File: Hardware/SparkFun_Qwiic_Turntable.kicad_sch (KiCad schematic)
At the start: 5 parts

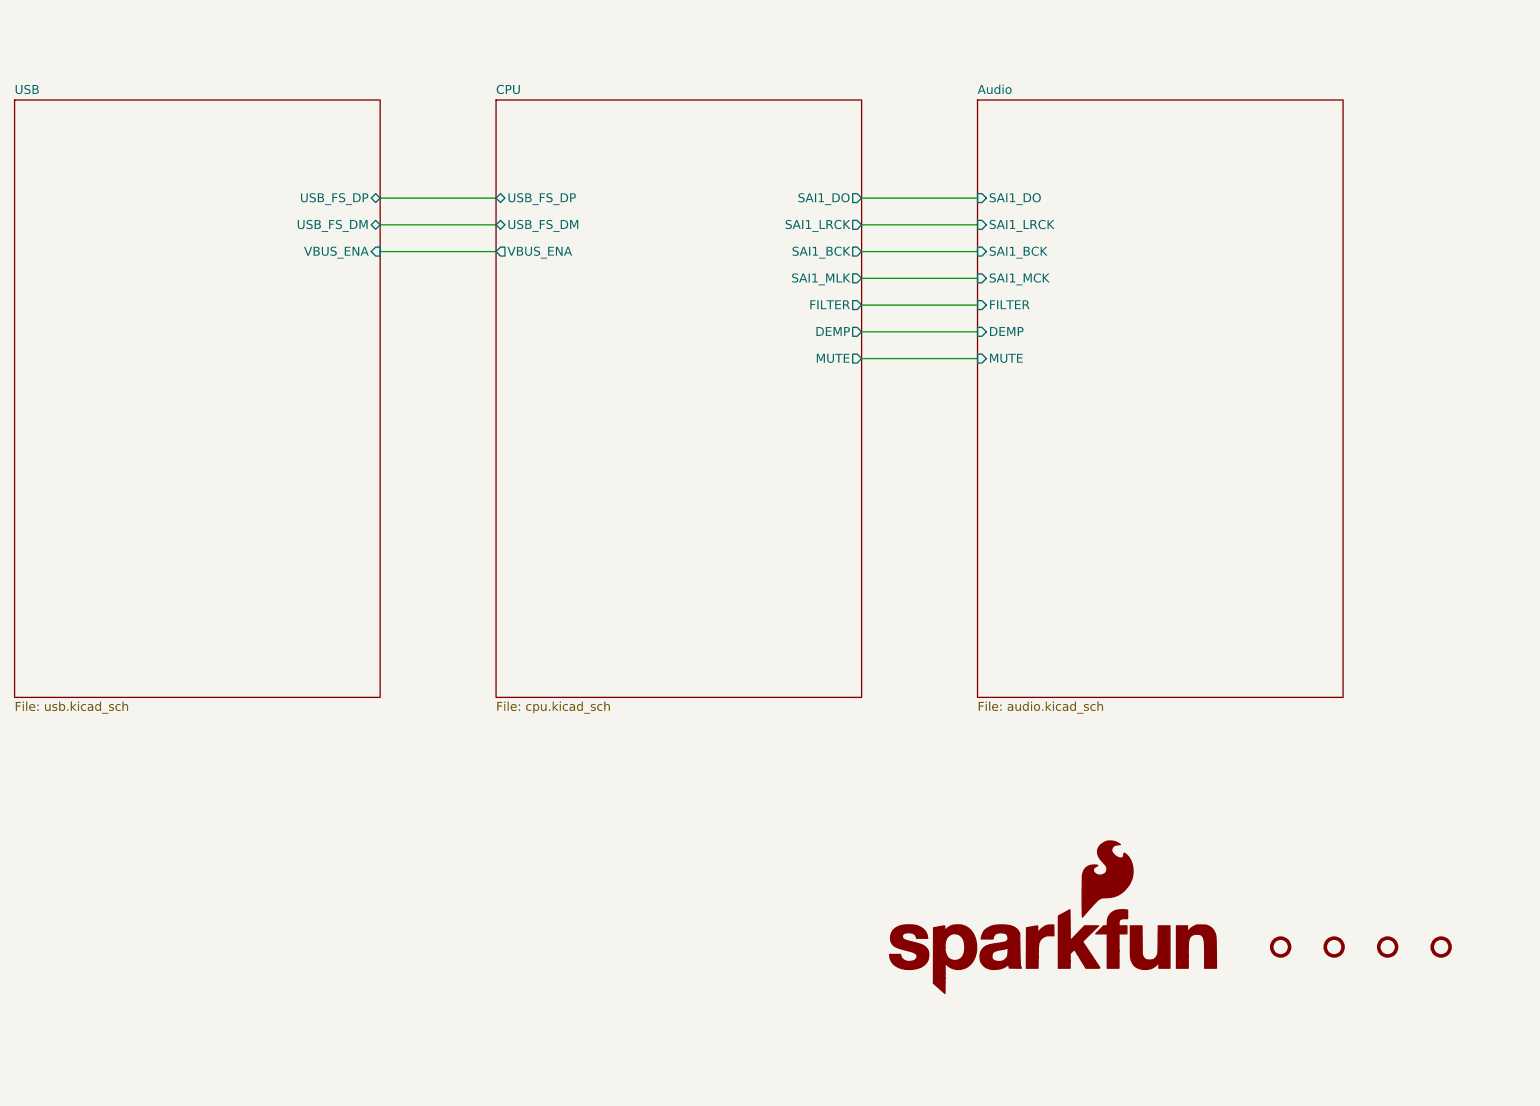
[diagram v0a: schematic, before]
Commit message: Restored VBUS load switch / limit circuit and changed most of the passives to 0402s.
Signed-off-by: Jamie Robertson <jrr@robertsonics.com>
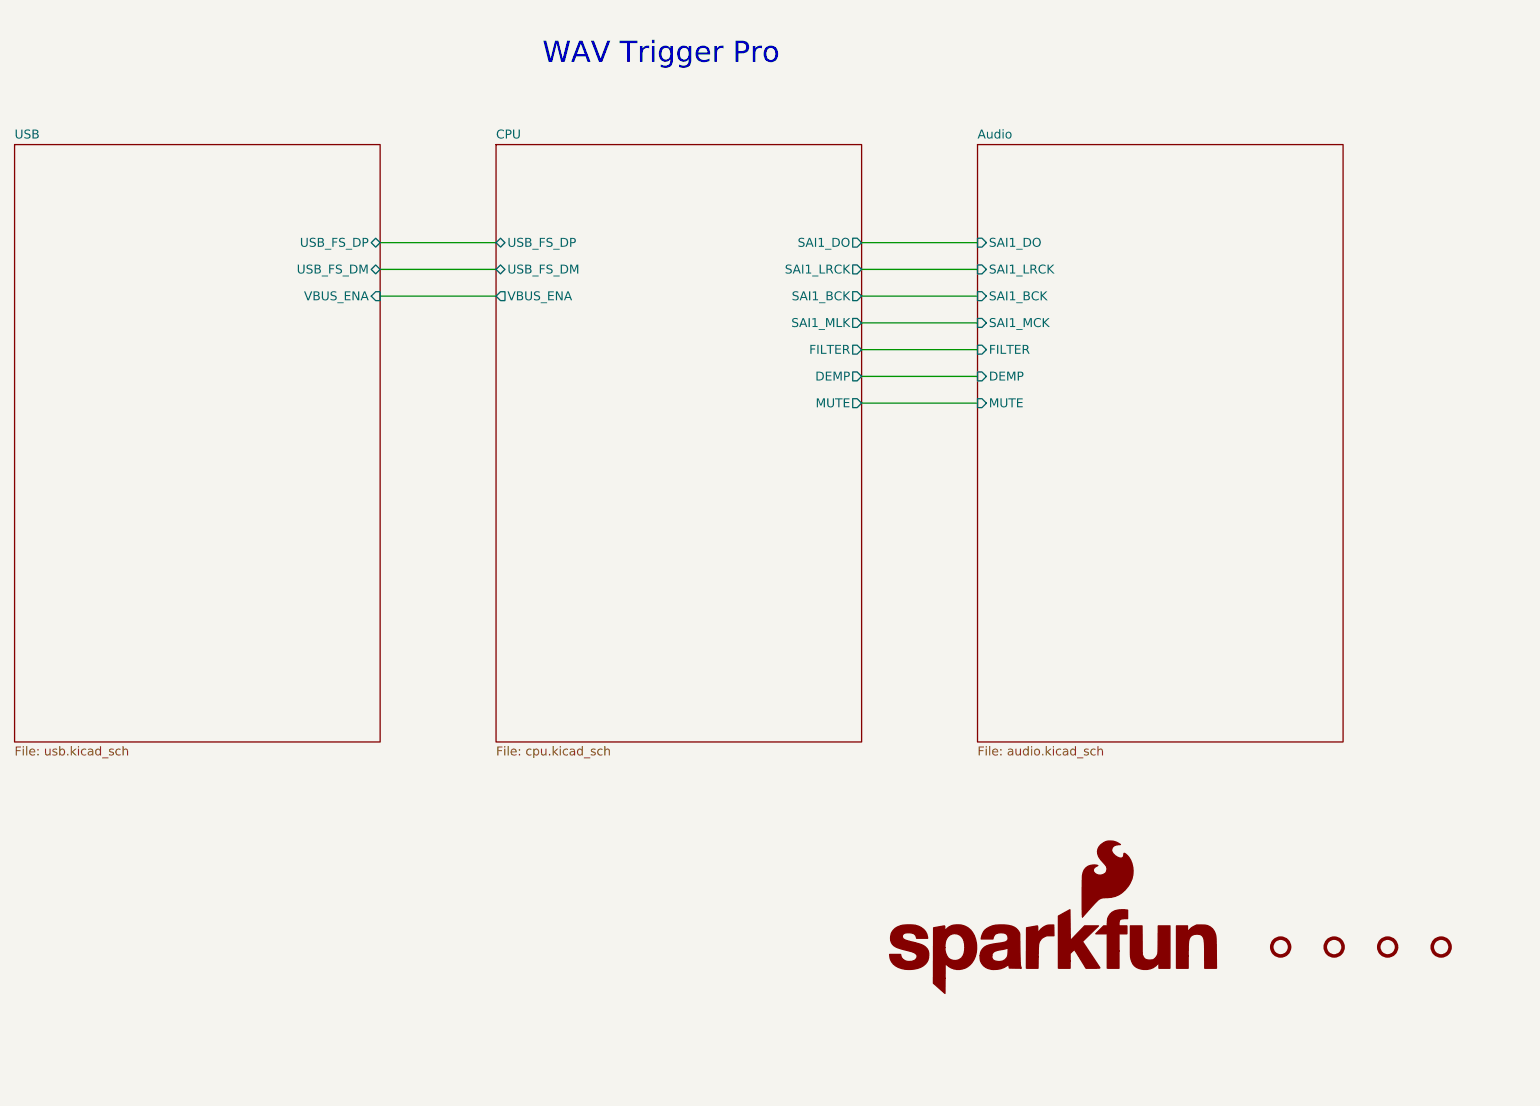
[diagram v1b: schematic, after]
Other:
- note added: "WAV Trigger Pro"
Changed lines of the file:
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@@
 	(wire
 		(pts
-			(xy 166.37 72.39) (xy 182.88 72.39)
-		)
-		(stroke
-			(width 0)
-			(type default)
-		)
-	)
-	(wire
-		(pts
-			(xy 97.79 60.96) (xy 114.3 60.96)
-		)
-		(stroke
-			(width 0)
-			(type default)
-		)
-	)
-	(wire
-		(pts
-			(xy 166.37 60.96) (xy 182.88 60.96)
-		)
-		(stroke
-			(width 0)
-			(type default)
-		)
-	)
-	(wire
-		(pts
-			(xy 97.79 64.77) (xy 114.3 64.77)
-		)
-		(stroke
-			(width 0)
-			(type default)
-		)
-	)
-	(wire
-		(pts
-			(xy 166.37 57.15) (xy 182.88 57.15)
-		)
-		(stroke
-			(width 0)
-			(type default)
-		)
-	)
-	(wire
-		(pts
-			(xy 97.79 57.15) (xy 114.3 57.15)
-		)
-		(stroke
-			(width 0)
-			(type default)
-		)
-	)
-	(wire
-		(pts
-			(xy 166.37 64.77) (xy 182.88 64.77)
-		)
-		(stroke
-			(width 0)
-			(type default)
-		)
-	)
-	(wire
-		(pts
-			(xy 166.37 76.2) (xy 182.88 76.2)
-		)
-		(stroke
-			(width 0)
-			(type default)
-		)
-	)
-	(wire
-		(pts
-			(xy 166.37 80.01) (xy 182.88 80.01)
-		)
-		(stroke
-			(width 0)
-			(type default)
-		)
-	)
-	(wire
-		(pts
-			(xy 166.37 68.58) (xy 182.88 68.58)
-		)
-		(stroke
-			(width 0)
-			(type default)
+			(xy 166.37 78.74) (xy 182.88 78.74)
+		)
+		(stroke
+			(width 0)
+			(type default)
+		)
+	)
+	(wire
+		(pts
+			(xy 97.79 67.31) (xy 114.3 67.31)
+		)
+		(stroke
+			(width 0)
+			(type default)
+		)
+	)
+	(wire
+		(pts
+			(xy 166.37 67.31) (xy 182.88 67.31)
+		)
+		(stroke
+			(width 0)
+			(type default)
+		)
+	)
+	(wire
+		(pts
+			(xy 97.79 71.12) (xy 114.3 71.12)
+		)
+		(stroke
+			(width 0)
+			(type default)
+		)
+	)
+	(wire
+		(pts
+			(xy 166.37 63.5) (xy 182.88 63.5)
+		)
+		(stroke
+			(width 0)
+			(type default)
+		)
+	)
+	(wire
+		(pts
+			(xy 97.79 63.5) (xy 114.3 63.5)
+		)
+		(stroke
+			(width 0)
+			(type default)
+		)
+	)
+	(wire
+		(pts
+			(xy 166.37 71.12) (xy 182.88 71.12)
+		)
+		(stroke
+			(width 0)
+			(type default)
+		)
+	)
+	(wire
+		(pts
+			(xy 166.37 82.55) (xy 182.88 82.55)
+		)
+		(stroke
+			(width 0)
+			(type default)
+		)
+	)
+	(wire
+		(pts
+			(xy 166.37 86.36) (xy 182.88 86.36)
+		)
+		(stroke
+			(width 0)
+			(type default)
+		)
+	)
+	(wire
+		(pts
+			(xy 166.37 74.93) (xy 182.88 74.93)
+		)
+		(stroke
+			(width 0)
+			(type default)
+		)
+	)
+	(text "WAV Trigger Pro"
+		(exclude_from_sim no)
+		(at 120.904 38.354 0)
+		(effects
+			(font
+				(size 3 3)
+			)
+			(justify left bottom)
 		)
 	)
@@
 	)
 	(sheet
-		(at 114.3 43.18)
+		(at 114.3 49.53)
 		(size 52.07 85.09)
 		(fields_autoplaced yes)
@@
 		)
 		(property "Sheetname" "CPU"
-			(at 114.3 42.4684 0)
+			(at 114.3 48.8184 0)
 			(effects
 				(font
@@
 		)
 		(property "Sheetfile" "cpu.kicad_sch"
-			(at 114.3 128.8546 0)
+			(at 114.3 135.2046 0)
 			(effects
 				(font
@@
 		)
 		(pin "SAI1_DO" output
-			(at 166.37 57.15 0)
+			(at 166.37 63.5 0)
 			(effects
 				(font
@@
 		)
 		(pin "SAI1_LRCK" output
-			(at 166.37 60.96 0)
+			(at 166.37 67.31 0)
 			(effects
 				(font
@@
 		)
 		(pin "SAI1_BCK" output
-			(at 166.37 64.77 0)
+			(at 166.37 71.12 0)
 			(effects
 				(font
@@
 		)
 		(pin "SAI1_MLK" output
-			(at 166.37 68.58 0)
+			(at 166.37 74.93 0)
 			(effects
 				(font
@@
 		)
 		(pin "USB_FS_DM" bidirectional
-			(at 114.3 60.96 180)
+			(at 114.3 67.31 180)
 			(effects
 				(font
@@
 		)
 		(pin "VBUS_ENA" output
-			(at 114.3 64.77 180)
+			(at 114.3 71.12 180)
 			(effects
 				(font
@@
 		)
 		(pin "USB_FS_DP" bidirectional
-			(at 114.3 57.15 180)
+			(at 114.3 63.5 180)
 			(effects
 				(font
@@
 		)
 		(pin "FILTER" output
-			(at 166.37 72.39 0)
+			(at 166.37 78.74 0)
 			(effects
 				(font
@@
 		)
 		(pin "DEMP" output
-			(at 166.37 76.2 0)
+			(at 166.37 82.55 0)
 			(effects
 				(font
@@
 		)
 		(pin "MUTE" output
-			(at 166.37 80.01 0)
+			(at 166.37 86.36 0)
 			(effects
 				(font
@@
 	)
 	(sheet
-		(at 45.72 43.18)
+		(at 45.72 49.53)
 		(size 52.07 85.09)
 		(fields_autoplaced yes)
@@
 		)
 		(property "Sheetname" "USB"
-			(at 45.72 42.4684 0)
+			(at 45.72 48.8184 0)
 			(effects
 				(font
@@
 		)
 		(property "Sheetfile" "usb.kicad_sch"
-			(at 45.72 128.8546 0)
+			(at 45.72 135.2046 0)
 			(effects
 				(font
@@
 			)
 		)
+		(pin "VBUS_ENA" input
+			(at 97.79 71.12 0)
+			(effects
+				(font
+					(size 1.27 1.27)
+				)
+				(justify right)
+			)
+		)
+		(pin "USB_FS_DM" bidirectional
+			(at 97.79 67.31 0)
+			(effects
+				(font
+					(size 1.27 1.27)
+				)
+				(justify right)
+			)
+		)
 		(pin "USB_FS_DP" bidirectional
-			(at 97.79 57.15 0)
-			(effects
-				(font
-					(size 1.27 1.27)
-				)
-				(justify right)
-			)
-		)
-		(pin "USB_FS_DM" bidirectional
-			(at 97.79 60.96 0)
-			(effects
-				(font
-					(size 1.27 1.27)
-				)
-				(justify right)
-			)
-		)
-		(pin "VBUS_ENA" input
-			(at 97.79 64.77 0)
+			(at 97.79 63.5 0)
 			(effects
 				(font
@@
 	)
 	(sheet
-		(at 182.88 43.18)
+		(at 182.88 49.53)
 		(size 52.07 85.09)
 		(fields_autoplaced yes)
@@
 		)
 		(property "Sheetname" "Audio"
-			(at 182.88 42.4684 0)
+			(at 182.88 48.8184 0)
 			(effects
 				(font
@@
 		)
 		(property "Sheetfile" "audio.kicad_sch"
-			(at 182.88 128.8546 0)
+			(at 182.88 135.2046 0)
 			(effects
 				(font
@@
 		)
 		(pin "SAI1_LRCK" input
-			(at 182.88 60.96 180)
+			(at 182.88 67.31 180)
 			(effects
 				(font
@@
 		)
 		(pin "SAI1_DO" input
-			(at 182.88 57.15 180)
+			(at 182.88 63.5 180)
 			(effects
 				(font
@@
 		)
 		(pin "SAI1_BCK" input
-			(at 182.88 64.77 180)
+			(at 182.88 71.12 180)
 			(effects
 				(font
@@
 		)
 		(pin "SAI1_MCK" input
-			(at 182.88 68.58 180)
+			(at 182.88 74.93 180)
 			(effects
 				(font
@@
 		)
 		(pin "MUTE" input
-			(at 182.88 80.01 180)
+			(at 182.88 86.36 180)
 			(effects
 				(font
@@
 		)
 		(pin "FILTER" input
-			(at 182.88 72.39 180)
+			(at 182.88 78.74 180)
 			(effects
 				(font
@@
 		)
 		(pin "DEMP" input
-			(at 182.88 76.2 180)
-			(effects
-				(font
+			(at 182.88 82.55 180)
+			(effects
+				(font

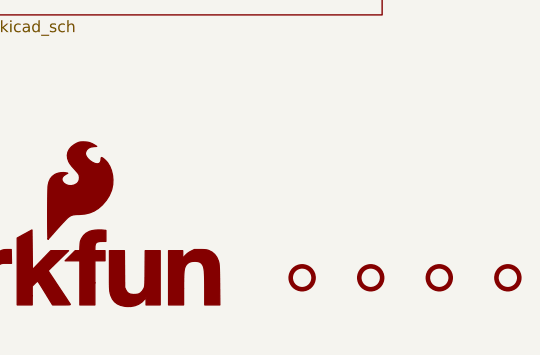
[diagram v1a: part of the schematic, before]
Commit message: Initial parts placement.
Signed-off-by: Jamie Robertson <jrr@robertsonics.com>
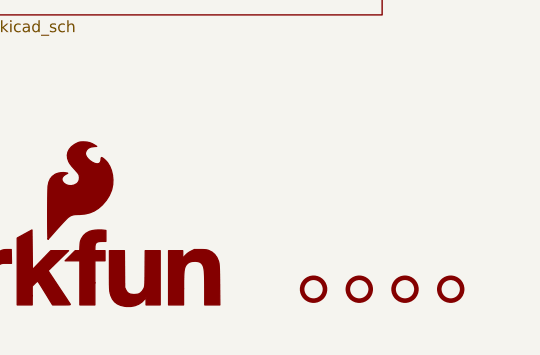
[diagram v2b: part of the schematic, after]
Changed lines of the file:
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@@
 	(symbol
 		(lib_id "SparkFun-Hardware:Standoff")
-		(at 241.3 163.83 0)
+		(at 232.41 165.1 0)
+		(unit 1)
+		(exclude_from_sim no)
+		(in_bom yes)
+		(on_board yes)
+		(dnp no)
+		(fields_autoplaced yes)
+		(property "Reference" "ST2"
+			(at 232.41 162.56 0)
+			(effects
+				(font
+					(size 1.27 1.27)
+				)
+				(hide yes)
+			)
+		)
+		(property "Value" "Standoff"
+			(at 232.41 167.64 0)
+			(effects
+				(font
+					(size 1.27 1.27)
+				)
+				(hide yes)
+			)
+		)
+		(property "Footprint" "SparkFun-Hardware:Standoff"
+			(at 232.41 170.18 0)
+			(effects
+				(font
+					(size 1.27 1.27)
+				)
+				(hide yes)
+			)
+		)
+		(property "Datasheet" "~"
+			(at 232.41 168.91 0)
+			(effects
+				(font
+					(size 1.27 1.27)
+				)
+				(hide yes)
+			)
+		)
+		(property "Description" "Drill holes for mechanically mounting via screws, standoffs, etc."
+			(at 232.41 165.1 0)
+			(effects
+				(font
+					(size 1.27 1.27)
+				)
+				(hide yes)
+			)
+		)
+		(instances
+			(project "SparkFun_Qwiic_Turntable"
+				(path "/4c0b78e3-6801-43aa-85ca-70880324c2bd"
+					(reference "ST2")
+					(unit 1)
+				)
+			)
+		)
+	)
+	(symbol
+		(lib_id "SparkFun-Hardware:Standoff")
+		(at 237.49 165.1 0)
 		(unit 1)
 		(exclude_from_sim no)
@@
 		(fields_autoplaced yes)
 		(property "Reference" "ST3"
-			(at 241.3 161.29 0)
-			(effects
-				(font
-					(size 1.27 1.27)
-				)
-				(hide yes)
-			)
-		)
-		(property "Value" "Standoff"
-			(at 241.3 166.37 0)
-			(effects
-				(font
-					(size 1.27 1.27)
-				)
-				(hide yes)
-			)
-		)
-		(property "Footprint" "SparkFun-Hardware:Standoff"
-			(at 241.3 168.91 0)
-			(effects
-				(font
-					(size 1.27 1.27)
-				)
-				(hide yes)
-			)
-		)
-		(property "Datasheet" "~"
-			(at 241.3 167.64 0)
-			(effects
-				(font
-					(size 1.27 1.27)
-				)
-				(hide yes)
-			)
-		)
-		(property "Description" ""
-			(at 241.3 163.83 0)
+			(at 237.49 162.56 0)
+			(effects
+				(font
+					(size 1.27 1.27)
+				)
+				(hide yes)
+			)
+		)
+		(property "Value" "Standoff"
+			(at 237.49 167.64 0)
+			(effects
+				(font
+					(size 1.27 1.27)
+				)
+				(hide yes)
+			)
+		)
+		(property "Footprint" "SparkFun-Hardware:Standoff"
+			(at 237.49 170.18 0)
+			(effects
+				(font
+					(size 1.27 1.27)
+				)
+				(hide yes)
+			)
+		)
+		(property "Datasheet" "~"
+			(at 237.49 168.91 0)
+			(effects
+				(font
+					(size 1.27 1.27)
+				)
+				(hide yes)
+			)
+		)
+		(property "Description" "Drill holes for mechanically mounting via screws, standoffs, etc."
+			(at 237.49 165.1 0)
 			(effects
 				(font
@@
 	(symbol
 		(lib_id "SparkFun-Hardware:Standoff")
-		(at 226.06 163.83 0)
+		(at 227.33 165.1 0)
 		(unit 1)
 		(exclude_from_sim no)
@@
 		(fields_autoplaced yes)
 		(property "Reference" "ST1"
-			(at 226.06 161.29 0)
-			(effects
-				(font
-					(size 1.27 1.27)
-				)
-				(hide yes)
-			)
-		)
-		(property "Value" "Standoff"
-			(at 226.06 166.37 0)
-			(effects
-				(font
-					(size 1.27 1.27)
-				)
-				(hide yes)
-			)
-		)
-		(property "Footprint" "SparkFun-Hardware:Standoff"
-			(at 226.06 168.91 0)
-			(effects
-				(font
-					(size 1.27 1.27)
-				)
-				(hide yes)
-			)
-		)
-		(property "Datasheet" "~"
-			(at 226.06 167.64 0)
-			(effects
-				(font
-					(size 1.27 1.27)
-				)
-				(hide yes)
-			)
-		)
-		(property "Description" ""
-			(at 226.06 163.83 0)
+			(at 227.33 162.56 0)
+			(effects
+				(font
+					(size 1.27 1.27)
+				)
+				(hide yes)
+			)
+		)
+		(property "Value" "Standoff"
+			(at 227.33 167.64 0)
+			(effects
+				(font
+					(size 1.27 1.27)
+				)
+				(hide yes)
+			)
+		)
+		(property "Footprint" "SparkFun-Hardware:Standoff"
+			(at 227.33 170.18 0)
+			(effects
+				(font
+					(size 1.27 1.27)
+				)
+				(hide yes)
+			)
+		)
+		(property "Datasheet" "~"
+			(at 227.33 168.91 0)
+			(effects
+				(font
+					(size 1.27 1.27)
+				)
+				(hide yes)
+			)
+		)
+		(property "Description" "Drill holes for mechanically mounting via screws, standoffs, etc."
+			(at 227.33 165.1 0)
 			(effects
 				(font
@@
 	(symbol
 		(lib_id "SparkFun-Hardware:Standoff")
-		(at 248.92 163.83 0)
+		(at 242.57 165.1 0)
 		(unit 1)
 		(exclude_from_sim no)
@@
 		(fields_autoplaced yes)
 		(property "Reference" "ST4"
-			(at 248.92 161.29 0)
-			(effects
-				(font
-					(size 1.27 1.27)
-				)
-				(hide yes)
-			)
-		)
-		(property "Value" "Standoff"
-			(at 248.92 166.37 0)
-			(effects
-				(font
-					(size 1.27 1.27)
-				)
-				(hide yes)
-			)
-		)
-		(property "Footprint" "SparkFun-Hardware:Standoff"
-			(at 248.92 168.91 0)
-			(effects
-				(font
-					(size 1.27 1.27)
-				)
-				(hide yes)
-			)
-		)
-		(property "Datasheet" "~"
-			(at 248.92 167.64 0)
-			(effects
-				(font
-					(size 1.27 1.27)
-				)
-				(hide yes)
-			)
-		)
-		(property "Description" ""
-			(at 248.92 163.83 0)
+			(at 242.57 162.56 0)
+			(effects
+				(font
+					(size 1.27 1.27)
+				)
+				(hide yes)
+			)
+		)
+		(property "Value" "Standoff"
+			(at 242.57 167.64 0)
+			(effects
+				(font
+					(size 1.27 1.27)
+				)
+				(hide yes)
+			)
+		)
+		(property "Footprint" "SparkFun-Hardware:Standoff"
+			(at 242.57 170.18 0)
+			(effects
+				(font
+					(size 1.27 1.27)
+				)
+				(hide yes)
+			)
+		)
+		(property "Datasheet" "~"
+			(at 242.57 168.91 0)
+			(effects
+				(font
+					(size 1.27 1.27)
+				)
+				(hide yes)
+			)
+		)
+		(property "Description" "Drill holes for mechanically mounting via screws, standoffs, etc."
+			(at 242.57 165.1 0)
 			(effects
 				(font
@@
 					(unit 1)
 				)
-			)
-		)
-	)
-	(symbol
-		(lib_id "SparkFun-Hardware:Standoff")
-		(at 233.68 163.83 0)
-		(unit 1)
-		(exclude_from_sim no)
-		(in_bom yes)
-		(on_board yes)
-		(dnp no)
-		(fields_autoplaced yes)
-		(property "Reference" "ST2"
-			(at 233.68 161.29 0)
-			(effects
-				(font
-					(size 1.27 1.27)
-				)
-				(hide yes)
-			)
-		)
-		(property "Value" "Standoff"
-			(at 233.68 166.37 0)
-			(effects
-				(font
-					(size 1.27 1.27)
-				)
-				(hide yes)
-			)
-		)
-		(property "Footprint" "SparkFun-Hardware:Standoff"
-			(at 233.68 168.91 0)
-			(effects
-				(font
-					(size 1.27 1.27)
-				)
-				(hide yes)
-			)
-		)
-		(property "Datasheet" "~"
-			(at 233.68 167.64 0)
-			(effects
-				(font
-					(size 1.27 1.27)
-				)
-				(hide yes)
-			)
-		)
-		(property "Description" ""
-			(at 233.68 163.83 0)
-			(effects
-				(font
-					(size 1.27 1.27)
-				)
-				(hide yes)
-			)
-		)
-		(instances
-			(project "SparkFun_Qwiic_Turntable"
-				(path "/4c0b78e3-6801-43aa-85ca-70880324c2bd"
-					(reference "ST2")
-					(unit 1)
-				)
